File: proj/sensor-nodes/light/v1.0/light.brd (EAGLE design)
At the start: 73 parts, among them J1 54602-908LF, J2 54602-908LF, U2 PCA9615DPJ, U3 MIC4680YM-TR, U4 LM2937IMP3.3NOPB, U5 SHT25, U6 CCS811, U7 T6713-5K, U8 HPP845E034R5

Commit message: added light sensor node v1.0
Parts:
- removed C10, C8: 0.1uF, openag-capacitors:C0603
- removed C2\1: 4.7uF, openag-capacitors:C0805
- removed R18: 4.7K, openag-resistors:R1206
- removed TP15, TP16, TP17, TP18, TP23, TP24, TP25, TP26, TP27, TP28: TPTP06R, openag-testpads:TP06R
- removed U6: CCS811, openag-sensors:CCS811
- removed U8: HPP845E034R5, openag-sensors:HTU20D(F)
- added TP6, TP7: TPTP06R, openag-testpads:TP06R
- U5: value SHT25 -> APDS-9250; device openag-sensors:SHT2X -> openag-sensors:APDS-9250
- U7: value T6713-5K -> TSL2591; device openag-sensors:T6713 -> openag-sensors:DFN6_TAOS
- moved TP20 39.3 mm to (97.0, 20.8), turned to 180 degrees
- moved TP19 31.8 mm to (97.0, 19.8), turned to 180 degrees
- moved C2 27.2 mm to (91.2, 39.4), turned to 180 degrees
- moved U5 26.2 mm to (93.5, 36.8)
- moved TP22 24.4 mm to (87.1, 14.5), turned to 180 degrees
- moved TP21 23.2 mm to (97.3, 13.2), turned to 180 degrees
- moved C7 15.2 mm to (92.7, 14.7), turned to 180 degrees
- moved U7 15.0 mm to (92.7, 18.0), turned to 270 degrees
- moved TP14 11.5 mm to (94.5, 41.1), turned to 180 degrees
- moved TP13 4.37 mm to (85.9, 35.8), turned to 180 degrees
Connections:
- removed net N$20: U6.4, U6.5
- removed net N$21: C8.1, R18.1, U6.2
- net +3V3: now also TP14.TP, TP21.TP, U5.3, U7.5; no longer C10.1, C2\1.1, R18.2, TP16.TP, TP20.TP, TP23.TP, TP27.TP, U5.5, U6.6, U7.3, U8.5
- net GND: now also TP13.TP, TP22.TP, U5.6, U7.3; no longer C10.2, C2\1.2, C8.2, TP15.TP, TP19.TP, TP24.TP, TP28.TP, U5.2, U6.1, U6.7, U6.EP, U7.4, U7.6, U8.2
- net SCL: now also TP20.TP, TP6.TP, U5.1, U7.1; no longer TP13.TP, TP18.TP, TP22.TP, TP26.TP, U5.6, U6.10, U7.2, U8.6
- net SDA: now also TP19.TP, TP7.TP, U5.2, U7.6; no longer TP14.TP, TP17.TP, TP21.TP, TP25.TP, U5.1, U6.9, U7.1, U8.1
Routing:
- net +3V3: track 343.5 -> 305.8 mm
- net SCL: track 131.4 -> 113.3 mm, vias 6 -> 2
- net SDA: track 130.4 -> 116.1 mm, vias 4 -> 2
- net N$21: track 5.85 -> 0.00 mm
- net N$20: track 0.60 -> 0.00 mm
- net GND: track 4.83 -> 4.52 mm, vias 9 -> 10
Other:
- board text added: "0x29"
- board text added: "0x52"
- board text added: "APDS9250 Light Sensor"
- board text added: "Light Sensor Node v1.0"
- board text added: "TS2591 Light Sensor"
- board text removed: "0x15"
- board text removed: "0x40"
- board text removed: "0x5A"
- board text removed: "Air Sensor Node v1.0"
- board text removed: "CCS811 CO2 Sensor"
- board text removed: "HTU20DF Temp/Hum"
- board text removed: "SHT25 Temp/Hum Sensor"
- board text removed: "T6713 CO2 Sensor"

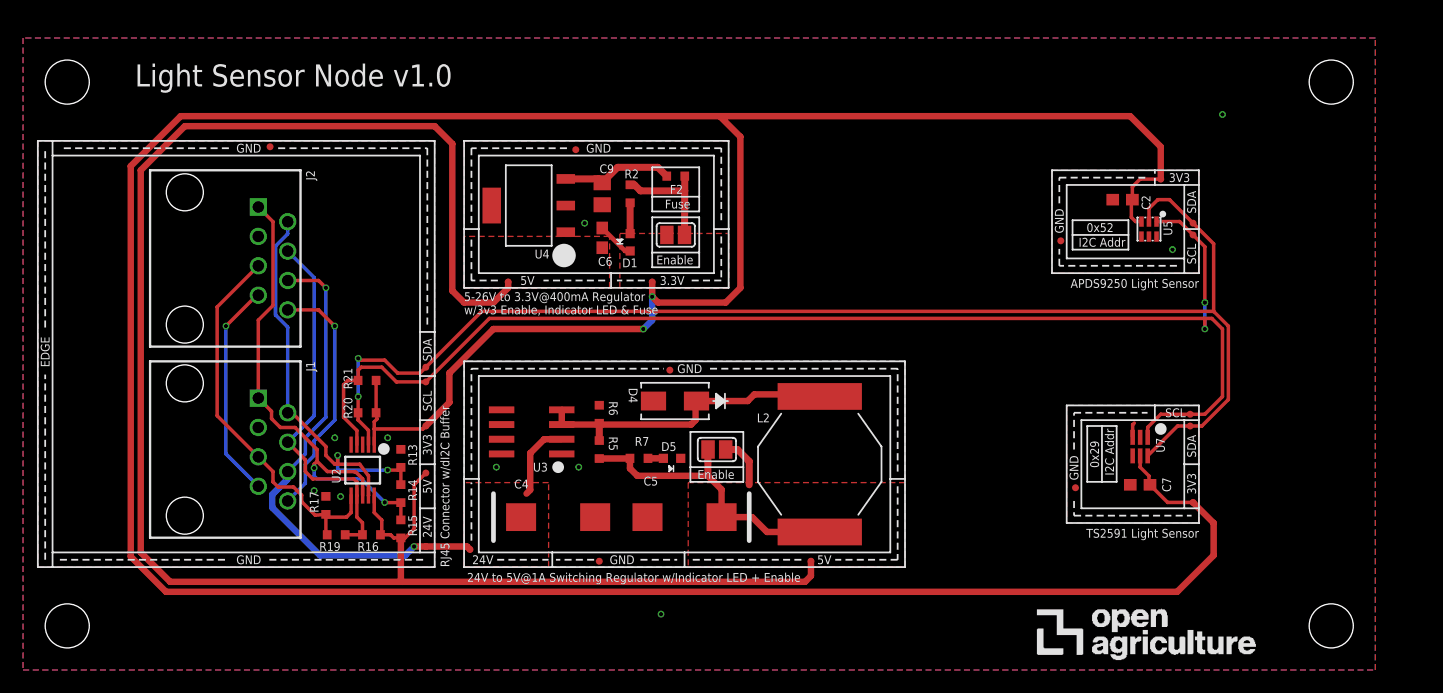
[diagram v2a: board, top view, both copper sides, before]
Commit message: added light and rj12 nodes, started working on light controller v2
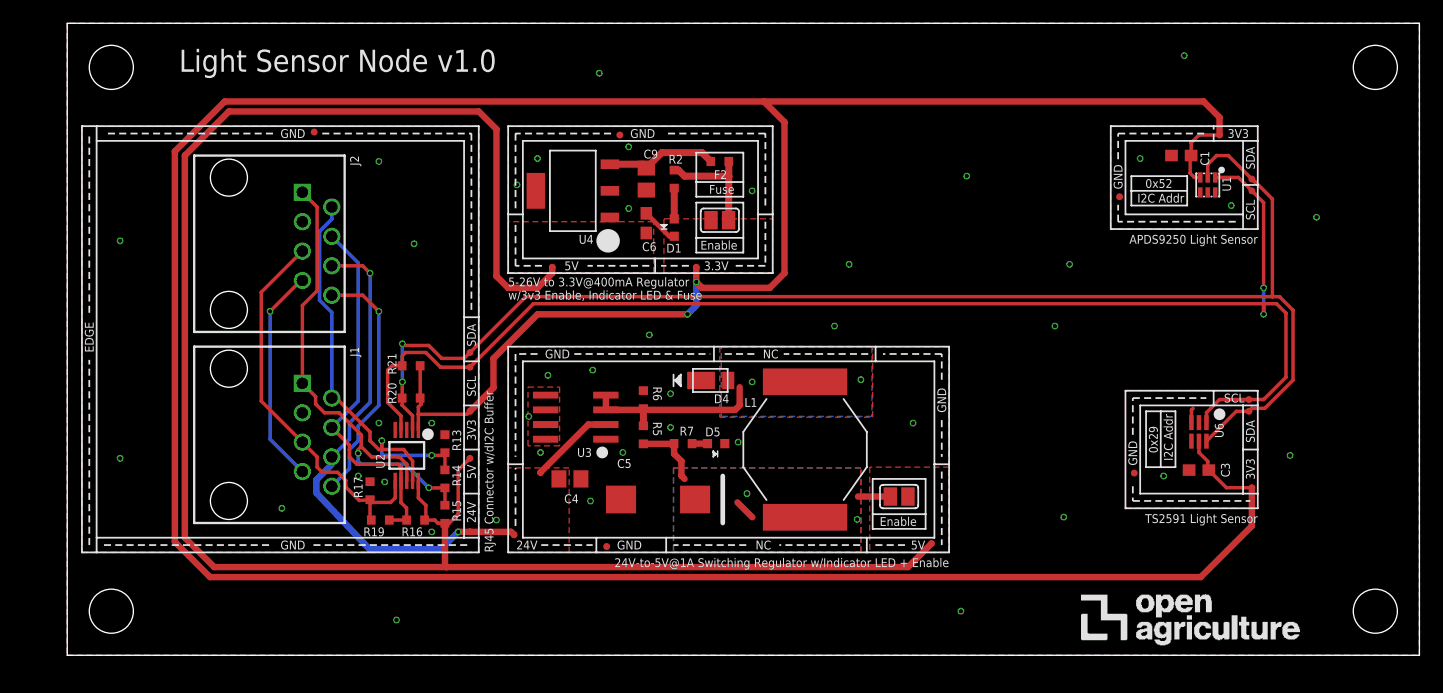
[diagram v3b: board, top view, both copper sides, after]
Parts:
- removed C2, C7: 0.1uF, openag-capacitors:C0603
- removed L2: 68uH, openag-inductors:UP2B
- removed SJ4: (no value), openag-connectors:SOLDERJUMPER_REFLOW_NOPASTE
- removed TP13, TP14, TP19, TP20, TP21, TP22, TP31: TPTP06R, openag-testpads:TP06R
- removed U5: APDS-9250, openag-sensors:APDS-9250
- removed U7: TSL2591, openag-sensors:DFN6_TAOS
- added C1, C3: 0.1uF, openag-capacitors:C0603
- added L1: 68uH, openag-inductors:UP2B
- added SJ2: (no value), openag-connectors:SOLDERJUMPER_REFLOW_NOPASTE
- added TP15, TP16, TP17, TP18, TP3, TP5: TPTP06R, openag-testpads:TP06R
- added U1: APDS-9250, openag-sensors:APDS-9250
- added U6: TSL2591, openag-sensors:DFN6_TAOS
- C4: device openag-capacitors:CT7343 -> openag-capacitors:C0805
- D4: value B260A-13-F -> SBR2A40P1-7; device openag-diodes:SMA -> openag-diodes:POWERDI123
- R13, R15, R16, R17: value NV -> 600
- R14, R19: value NV -> 120
- R2, R7: value 100 OHM -> 100
- R20, R21: value NV -> 10K
- moved TP12 74.0 mm to (99.6, 45.0)
- moved TP7 64.6 mm to (38.6, 10.4)
- moved TP6 57.4 mm to (46.6, 9.40)
- moved TP10 50.4 mm to (102.4, 41.1)
- moved TP11 41.7 mm to (90.9, 39.6)
- moved FRAME1 24.1 mm to (77.2, 3.30), turned to 0 degrees
- moved D1 4.02 mm to (52.5, 37.0)
- moved R2 4.02 mm to (52.5, 41.1)
- moved U3 4.02 mm to (43.9, 20.6)
- moved TP34 4.02 mm to (34.8, 17.0)
- moved D5 4.02 mm to (56.1, 18.3)
- moved J2 4.02 mm to (14.0, 35.6)
- moved R13 4.02 mm to (32.6, 18.3)
- moved R14 4.02 mm to (32.6, 15.2)
- moved R15 4.02 mm to (32.6, 12.2)
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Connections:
- removed net TAB: U4.4
- net +24V: now also C4.1, TP7.TP; no longer C4.+, TP12.TP
- net +3V3: now also C1.1, C3.1, TP12.TP, TP17.TP, U1.3, U6.5; no longer C2.1, C7.1, TP14.TP, TP21.TP, U5.3, U7.5
- net +5V: now also SJ2.2, TP5.TP; no longer SJ4.2, TP10.TP
- net GND: now also C1.2, C3.2, C4.2, D4.-, TP18.TP, TP6.TP, U1.6, U4.4, U6.3; no longer C2.2, C4.-, C7.2, D4.2, TP13.TP, TP22.TP, TP31.TP, U5.6, U7.3
- net N$31: now also D4.+, L1.1; no longer D4.1, L2.1
- net N$33: now also L1.2, SJ2.1; no longer L2.2, SJ4.1
- net SCL: now also TP16.TP, TP3.TP, U1.1, U6.1; no longer TP20.TP, TP6.TP, U5.1, U7.1
- net SDA: now also TP10.TP, TP15.TP, U1.2, U6.6; no longer TP19.TP, TP7.TP, U5.2, U7.6
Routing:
- net N$33: track 25.9 -> 10.7 mm, vias 0 -> 2
- net N$31: track 27.3 -> 16.2 mm, vias 0 -> 2
- net SDA: track 116.1 -> 120.7 mm
- net SCL: track 113.3 -> 117.7 mm
- net +3V3: track 305.8 -> 303.3 mm
- net +5V: track 162.2 -> 163.7 mm
- net +24V: track 50.5 -> 51.8 mm
- net GND: vias 10 -> 42
- added copper zone on layer 1, net N$31
- added copper zone on layer 16, net N$31
- added copper zone on layer 1, net N$33
- added copper zone on layer 16, net N$33
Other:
- board outline added: 116.8 x 54.6 mm
- board text added: "24V-to-5V@1A Switching Regulator w/Indicator LED + Enable"
- board text added: "NC"
- board text removed: "24V to 5V@1A Switching Regulator w/Indicator LED + Enable"
